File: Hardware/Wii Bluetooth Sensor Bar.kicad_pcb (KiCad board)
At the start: 2 copper layers, 32 x 35 mm, 13 parts, among them J1 LED_Left, J2 LED_Right, SW1 SW_Push, U1 J27H002, U2 LM1117-3.3

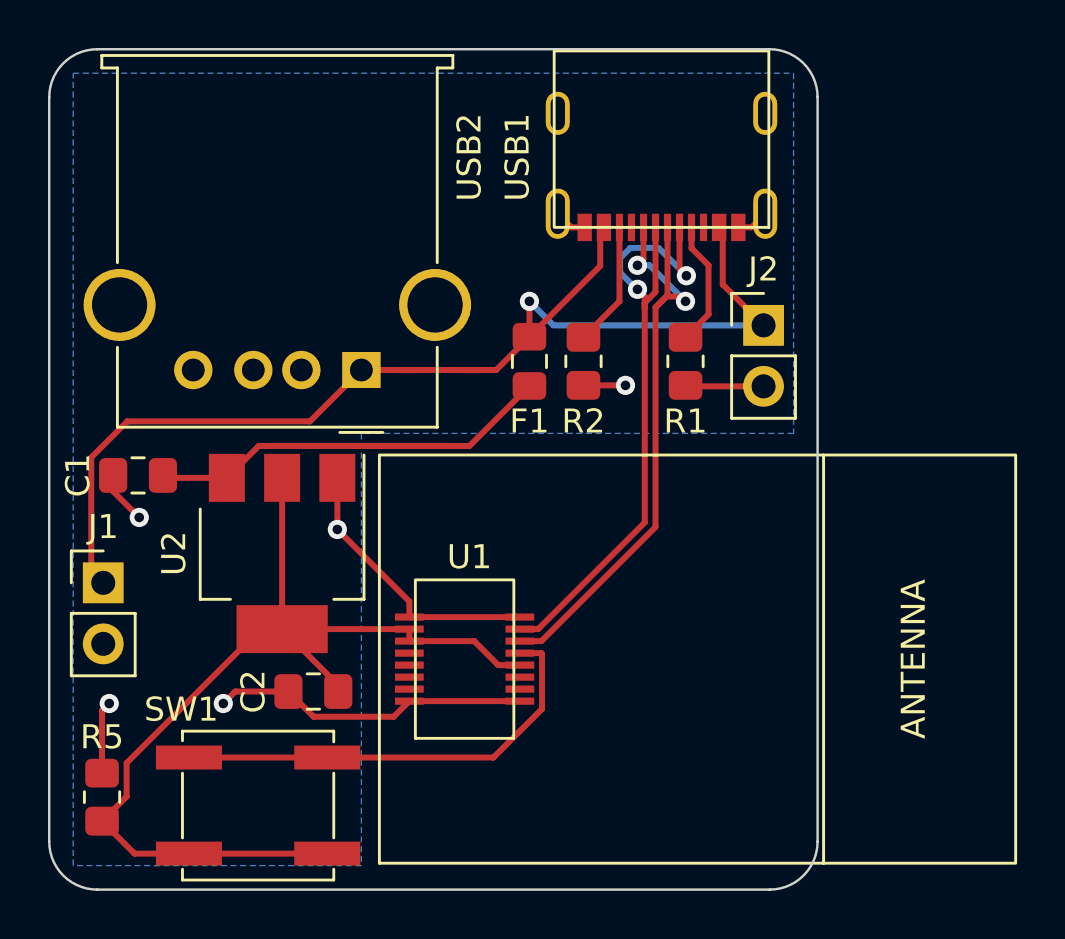
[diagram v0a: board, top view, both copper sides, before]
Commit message: Fix reversed bluetooth module connector
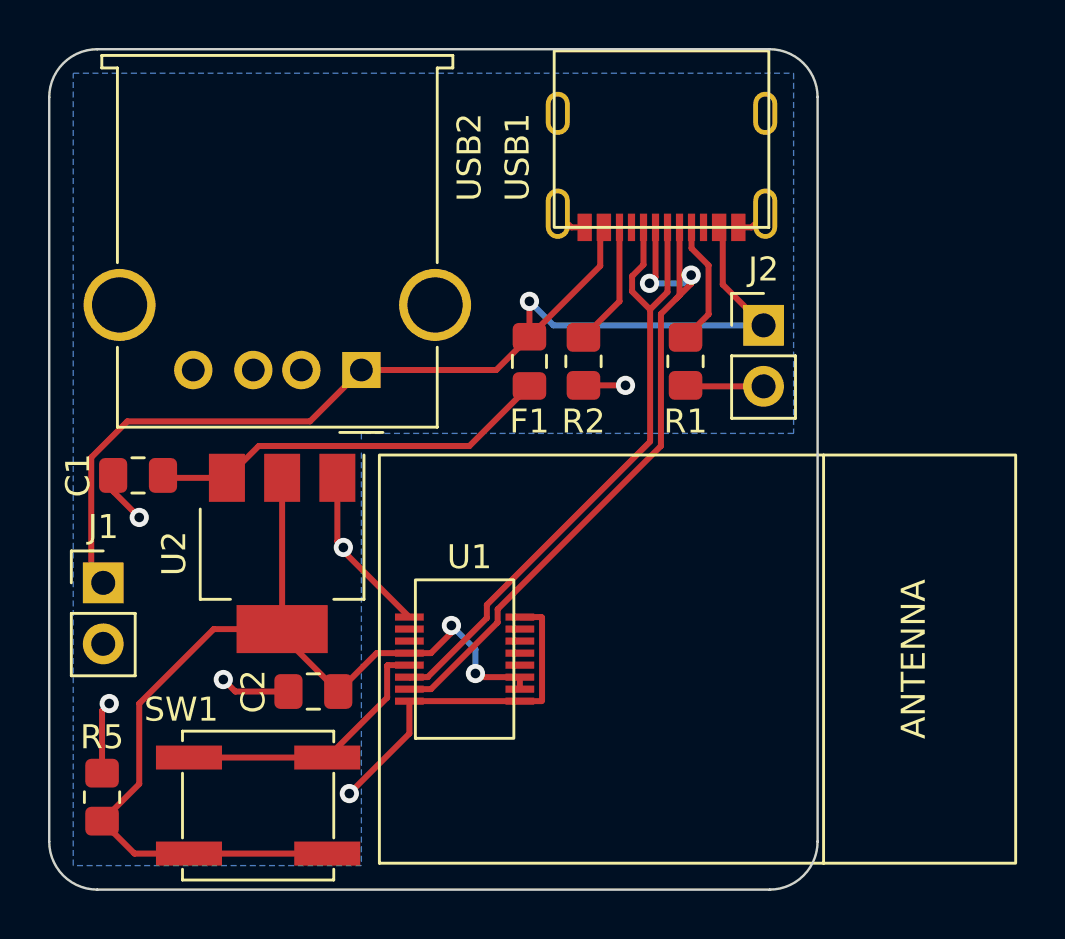
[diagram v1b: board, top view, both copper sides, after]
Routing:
- net Net-(SW1-Pad2): track 18.8 -> 11.6 mm
- net Net-(USB1-PadA7): track 27.6 -> 29.9 mm
- net Net-(USB1-PadA6): track 26.0 -> 27.6 mm, vias 2 -> 0
- net +3V3: track 42.3 -> 43.4 mm, vias 0 -> 2
- net GND: track 37.6 -> 37.4 mm, vias 5 -> 6

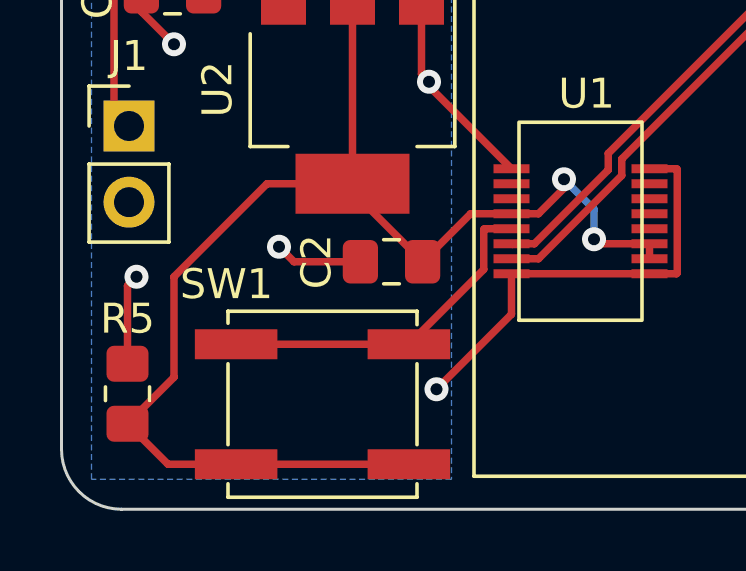
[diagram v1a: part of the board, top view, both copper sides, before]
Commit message: Fix incorrect sync button footprint
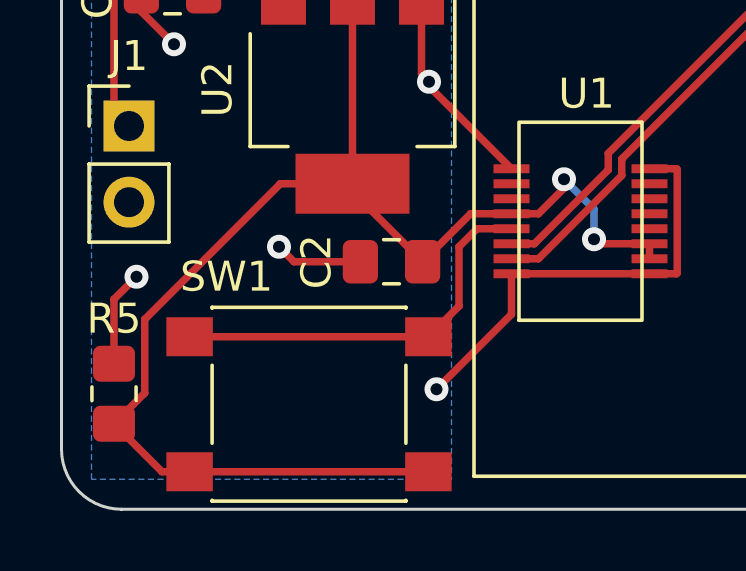
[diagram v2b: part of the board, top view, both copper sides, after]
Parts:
- SW1: footprint Button_Switch_SMD:SW_SPST_EVPBF -> Button_Switch_SMD:SW_SPST_PTS645
- moved R5 0.45 mm to (124.8, 107.2)
- moved SW1 0.45 mm to (131.2, 107.5)
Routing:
- net Net-(SW1-Pad2): track 11.6 -> 13.4 mm
- net +3V3: track 43.4 -> 44.6 mm

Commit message: Add PCB label text
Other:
- board text added: "Wii BT Sensor Bar Revision A Benjamin Owen 2022-07-08"
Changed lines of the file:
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@@
   (gr_line (start 153 111) (end 125 111) (layer "Edge.Cuts") (width 0.1))
   (gr_arc (start 155 109) (mid 154.414214 110.414214) (end 153 111) (layer "Edge.Cuts") (width 0.1))
+  (gr_text "Wii BT Sensor Bar\nRevision A\nBenjamin Owen\n2022-07-08" (at 146.5 99.75 270) (layer "B.SilkS")
+    (effects (font (size 1.5 1.5) (thickness 0.3)) (justify mirror))
+  )
   (segment (start 131.725 92.525) (end 130.4 93.85) (width 0.25) (layer "F.Cu") (net 1))
   (segment (start 143 90.025) (end 140.5 92.525) (width 0.25) (layer "F.Cu") (net 1))

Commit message: Fix #1
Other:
- board text added: "Wii BT Sensor Bar Revision B Benjamin Owen 2022-07-27"
- board text removed: "Wii BT Sensor Bar Revision A Benjamin Owen 2022-07-08"
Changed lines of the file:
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@@
     )
     (fp_rect (start -0.15 -4.75) (end 8.79 2.6) (layer "F.SilkS") (width 0.12) (fill none))
+    (pad "" np_thru_hole circle (at 7.21 -3.68 180) (size 0.65 0.65) (drill 0.65) (layers F&B.Cu *.Mask))
+    (pad "" np_thru_hole circle (at 1.43 -3.68 180) (size 0.65 0.65) (drill 0.65) (layers F&B.Cu *.Mask))
     (pad "A1" smd rect (at 0.97 -4.75 180) (size 0.3 1.14) (layers "F.Cu" "F.Paste" "F.Mask")
       (net 2 "GND") (pinfunction "GND") (pintype "passive"))
@@
     (pad "B12" smd rect (at 1.27 -4.75 180) (size 0.3 1.14) (layers "F.Cu" "F.Paste" "F.Mask")
       (net 2 "GND") (pinfunction "GND") (pintype "passive"))
+    (pad "S1" thru_hole oval (at 0 0 180) (size 1 1.8) (drill oval 0.6 1.4) (layers *.Cu *.Mask)
+      (net 2 "GND") (pinfunction "SHIELD") (pintype "passive"))
+    (pad "S1" thru_hole oval (at 0 -4.18 180) (size 1 2.1) (drill oval 0.6 1.7) (layers *.Cu *.Mask)
+      (net 2 "GND") (pinfunction "SHIELD") (pintype "passive"))
     (pad "S1" thru_hole oval (at 8.64 0 180) (size 1 1.8) (drill oval 0.6 1.4) (layers *.Cu *.Mask)
       (net 2 "GND") (pinfunction "SHIELD") (pintype "passive"))
     (pad "S1" thru_hole oval (at 8.64 -4.18 180) (size 1 2.1) (drill oval 0.6 1.7) (layers *.Cu *.Mask)
       (net 2 "GND") (pinfunction "SHIELD") (pintype "passive"))
-    (pad "S1" thru_hole oval (at 0 -4.18 180) (size 1 2.1) (drill oval 0.6 1.7) (layers *.Cu *.Mask)
-      (net 2 "GND") (pinfunction "SHIELD") (pintype "passive"))
-    (pad "S1" thru_hole oval (at 0 0 180) (size 1 1.8) (drill oval 0.6 1.4) (layers *.Cu *.Mask)
-      (net 2 "GND") (pinfunction "SHIELD") (pintype "passive"))
-    (model "${KICAD6_3DMODEL_DIR}/Connector_USB.3dshapes/USB_Micro-B_Molex_47346-0001.wrl"
-      (offset (xyz 4 2.5 0))
-      (scale (xyz 1.2 1.3 1))
-      (rotate (xyz 0 0 0))
-    )
   )
   (footprint "Connector_PinHeader_2.54mm:PinHeader_1x02_P2.54mm_Vertical" (layer "F.Cu")
@@
       (connect_pads (clearance 0))
       (min_thickness 0.254)
-      (keepout (tracks allowed) (vias allowed) (pads allowed ) (copperpour not_allowed) (footprints allowed))
+      (keepout (tracks allowed) (vias allowed) (pads allowed) (copperpour not_allowed) (footprints allowed))
       (fill (thermal_gap 0.508) (thermal_bridge_width 0.508))
       (polygon
@@
   (gr_line (start 153 111) (end 125 111) (layer "Edge.Cuts") (width 0.1))
   (gr_arc (start 155 109) (mid 154.414214 110.414214) (end 153 111) (layer "Edge.Cuts") (width 0.1))
-  (gr_text "Wii BT Sensor Bar\nRevision A\nBenjamin Owen\n2022-07-08" (at 146.5 99.75 270) (layer "B.SilkS")
-    (effects (font (size 1.5 1.5) (thickness 0.3)) (justify mirror))
+  (gr_text "Wii BT Sensor Bar\nRevision B\nBenjamin Owen\n2022-07-27" (at 154.5 96.5) (layer "B.SilkS")
+    (effects (font (size 1.3 1.3) (thickness 0.25)) (justify left mirror))
   )
   (segment (start 131.725 92.525) (end 130.4 93.85) (width 0.25) (layer "F.Cu") (net 1))

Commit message: Add Ben's Universe logo #3
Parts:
- added G***: LOGO, Logos:BU-Logo-10mm, B.Cu at (149.2, 105.0)
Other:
- board text added: "Wii BT Sensor Bar Revision B Benjamin Owen"
- board text removed: "Wii BT Sensor Bar Revision B Benjamin Owen 2022-07-27"

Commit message: Update versioning
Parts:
- moved U1 0.25 mm to (137.8, 103.2)
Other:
- board text added: "Wii BT Sensor Bar Revision 1.1 Benjamin Owen"
- board text removed: "Wii BT Sensor Bar Revision B Benjamin Owen"

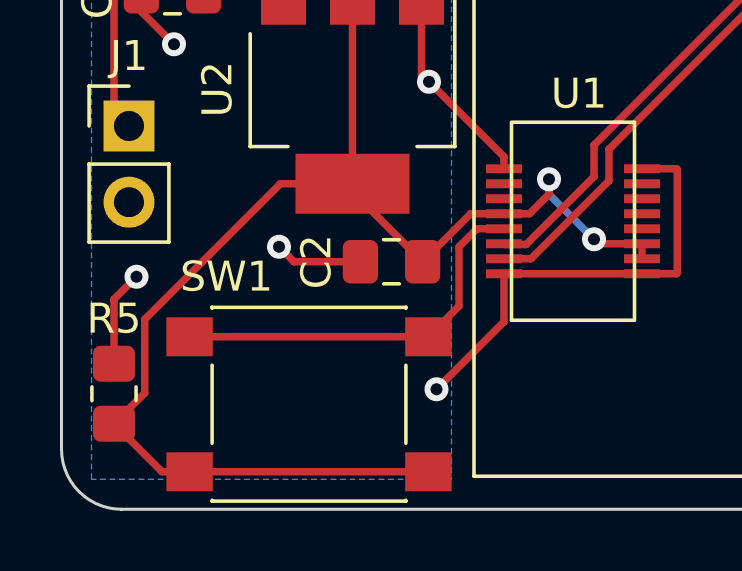
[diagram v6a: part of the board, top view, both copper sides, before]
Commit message: Fix bad pulldown resistor
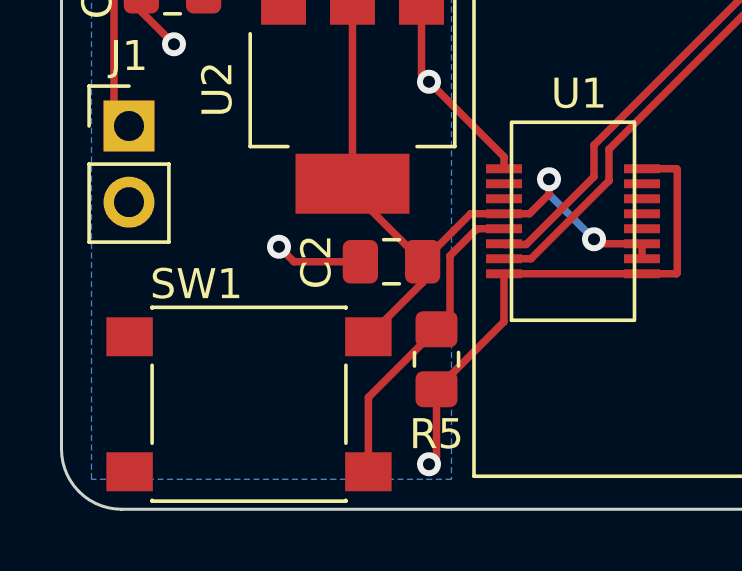
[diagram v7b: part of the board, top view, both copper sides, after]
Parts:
- moved R5 10.8 mm to (135.5, 106.0), turned to -90 degrees
- moved SW1 2.00 mm to (129.2, 107.5), turned to 0 degrees
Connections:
- R5 pad 1: +3V3 -> Net-(U1-Pad12)
- SW1 pad 2: Net-(SW1-Pad2) -> Net-(U1-Pad12)
- U1 pad 12: Net-(SW1-Pad2) -> Net-(U1-Pad12)
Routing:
- net +3V3: track 44.1 -> 23.5 mm
- net Net-(SW1-Pad2): track 13.1 -> 0.00 mm
- net Net-(U1-Pad12): track 0.00 -> 10.5 mm
- net GND: track 38.1 -> 37.4 mm, vias 6 -> 5
